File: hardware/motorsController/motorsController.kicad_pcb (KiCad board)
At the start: 2 copper layers, 166.1 x 53.6 mm, 48 parts, among them J1 batery_connector, J10 batery_connector, J11 Conn_01x04, J2 Screw_Terminal_01x01, J3 Screw_Terminal_01x01, J4 Screw_Terminal_01x01, J5 Screw_Terminal_01x01, J6 Screw_Terminal_01x01, J7 Screw_Terminal_01x01, J8 Screw_Terminal_01x01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

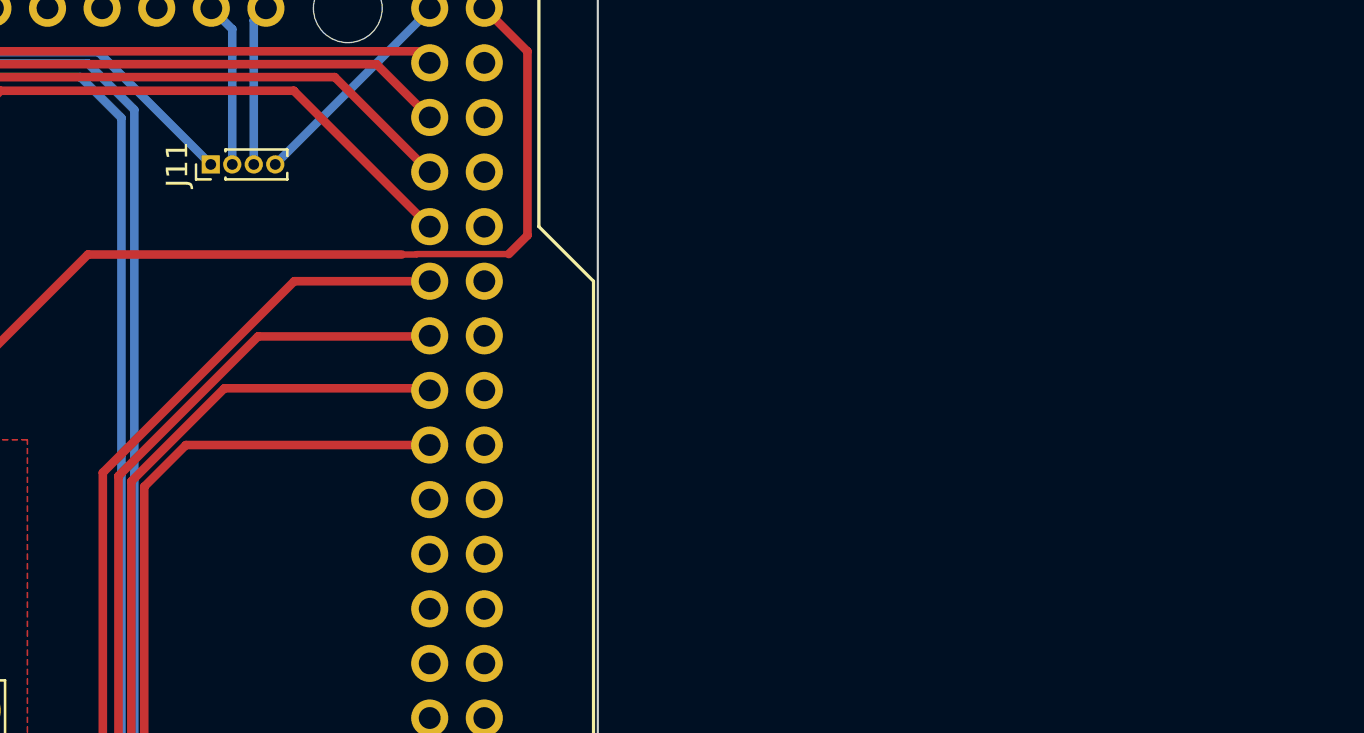
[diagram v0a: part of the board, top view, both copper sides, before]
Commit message: layout filters for an encoder
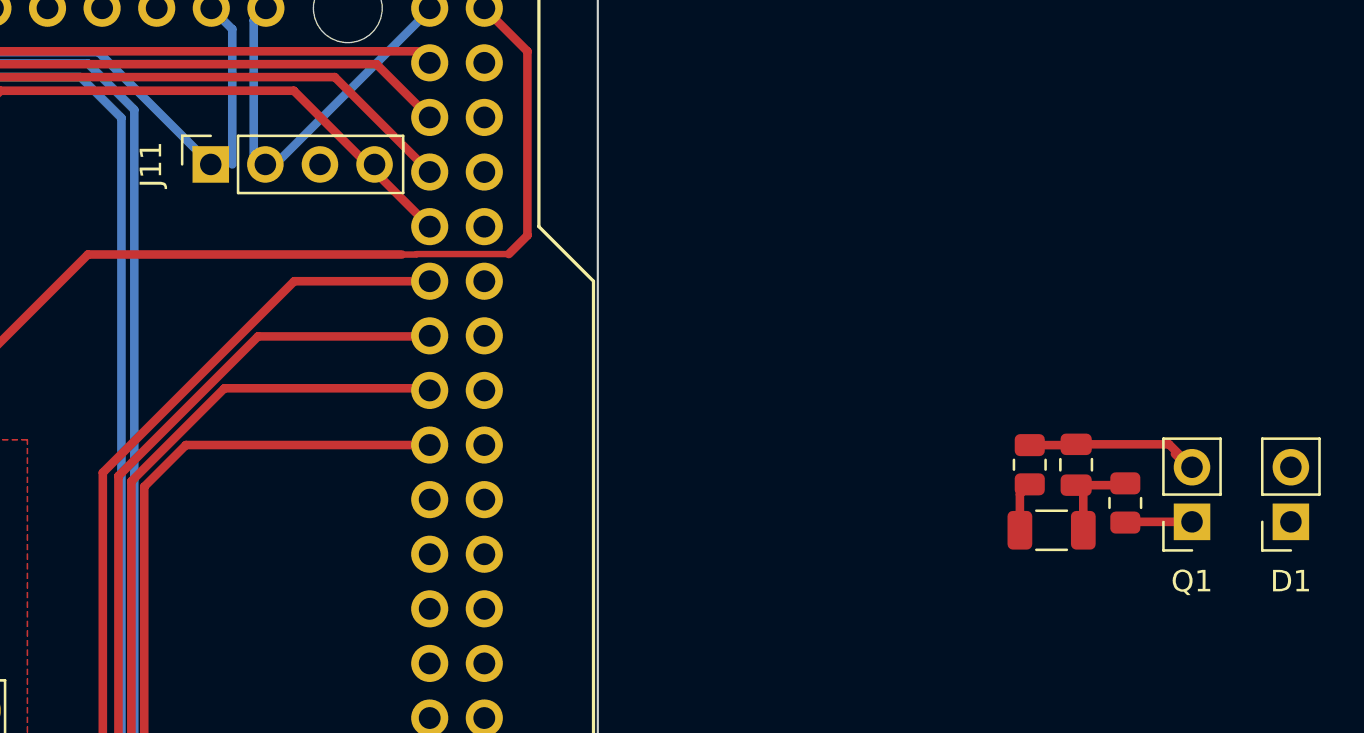
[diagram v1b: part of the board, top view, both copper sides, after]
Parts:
- added C5: 300pF, Capacitor_SMD:C_0805_2012Metric, F.Cu at (221.2, 48.3)
- added C6: 82nF, Capacitor_SMD:C_1206_3216Metric, F.Cu at (220.1, 51.3)
- added D1: LED, Connector_PinSocket_2.54mm:PinSocket_1x02_P2.54mm_Vertical, F.Cu at (231.2, 50.9)
- added Q1: Q_Photo_NPN, Connector_PinSocket_2.54mm:PinSocket_1x02_P2.54mm_Vertical, F.Cu at (226.6, 50.9)
- added R30: 2M, Resistor_SMD:R_0805_2012Metric, F.Cu at (219.1, 48.3)
- added Re: 2M, Resistor_SMD:R_0805_2012Metric, F.Cu at (223.5, 50.0)
- J11: footprint Connector_PinHeader_1.00mm:PinHeader_1x04_P1.00mm_Vertical -> Connector_PinSocket_2.54mm:PinSocket_1x04_P2.54mm_Vertical
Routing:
- net GND: track 638.6 -> 647.6 mm
- net Net-(C5-Pad1): track 0.00 -> 4.56 mm
- net Net-(Q1-Pad1): track 0.00 -> 3.13 mm
- net /front_right_encoder/out: track 0.00 -> 2.33 mm

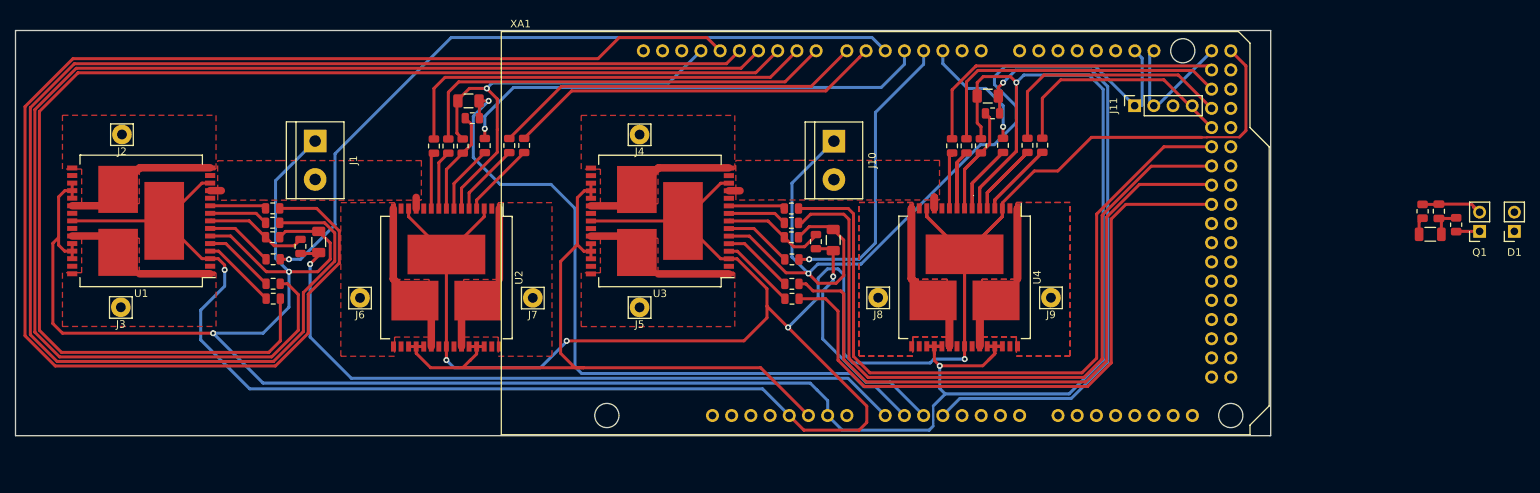
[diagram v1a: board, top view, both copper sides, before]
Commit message: connect encoder to arduino
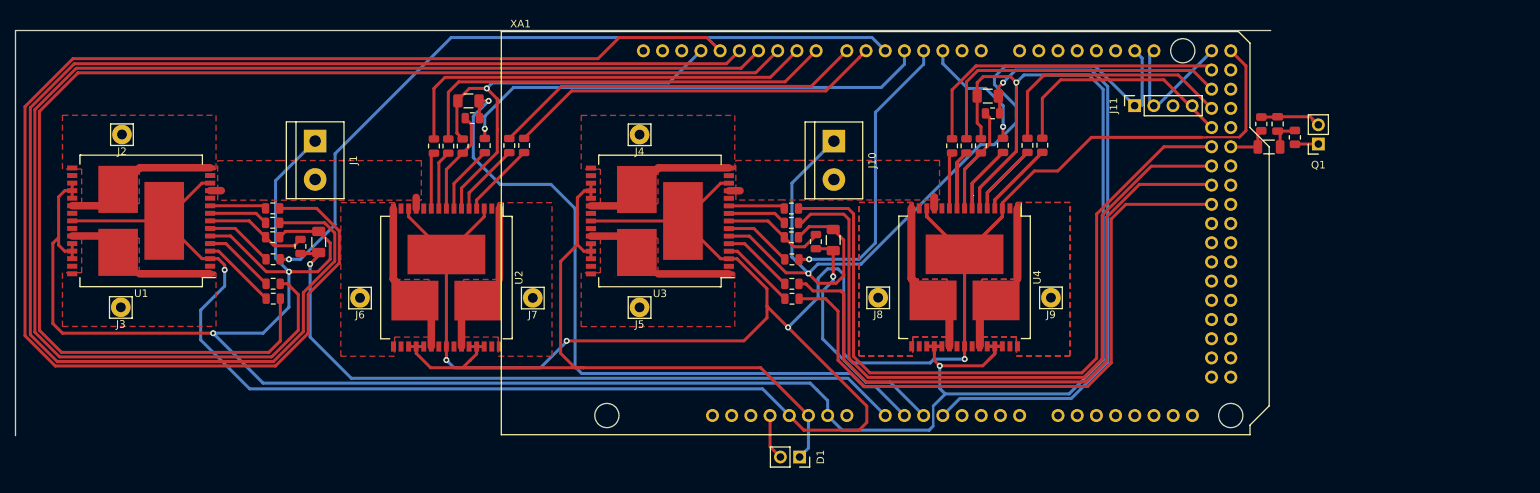
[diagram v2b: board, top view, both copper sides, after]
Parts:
- moved D1 99.2 mm to (136.7, 80.8), turned to 270 degrees
- moved C5 24.3 mm to (199.9, 36.7)
- moved C6 24.3 mm to (198.8, 39.8)
- moved R29 24.3 mm to (202.2, 38.5)
- moved Q1 24.3 mm to (205.3, 39.4)
- moved R30 24.3 mm to (197.7, 36.7)
- renumbered Re to R29
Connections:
- C6 pad 1: /front_right_encoder/out -> /front_right_encoder
- R30 pad 1: /front_right_encoder/out -> /front_right_encoder
- XA1 pad 3V3: Net-(XA1-Pad3V3) -> +3V3
- XA1 pad D31: Net-(XA1-PadD31) -> /front_right_encoder
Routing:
- net +3V3: track 0.00 -> 6.06 mm
- net GND: track 647.6 -> 653.6 mm
- net /front_right_encoder: track 0.00 -> 5.92 mm
- net /front_right_encoder/out: track 2.33 -> 0.00 mm
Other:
- outline, holes or cut-outs redrawn

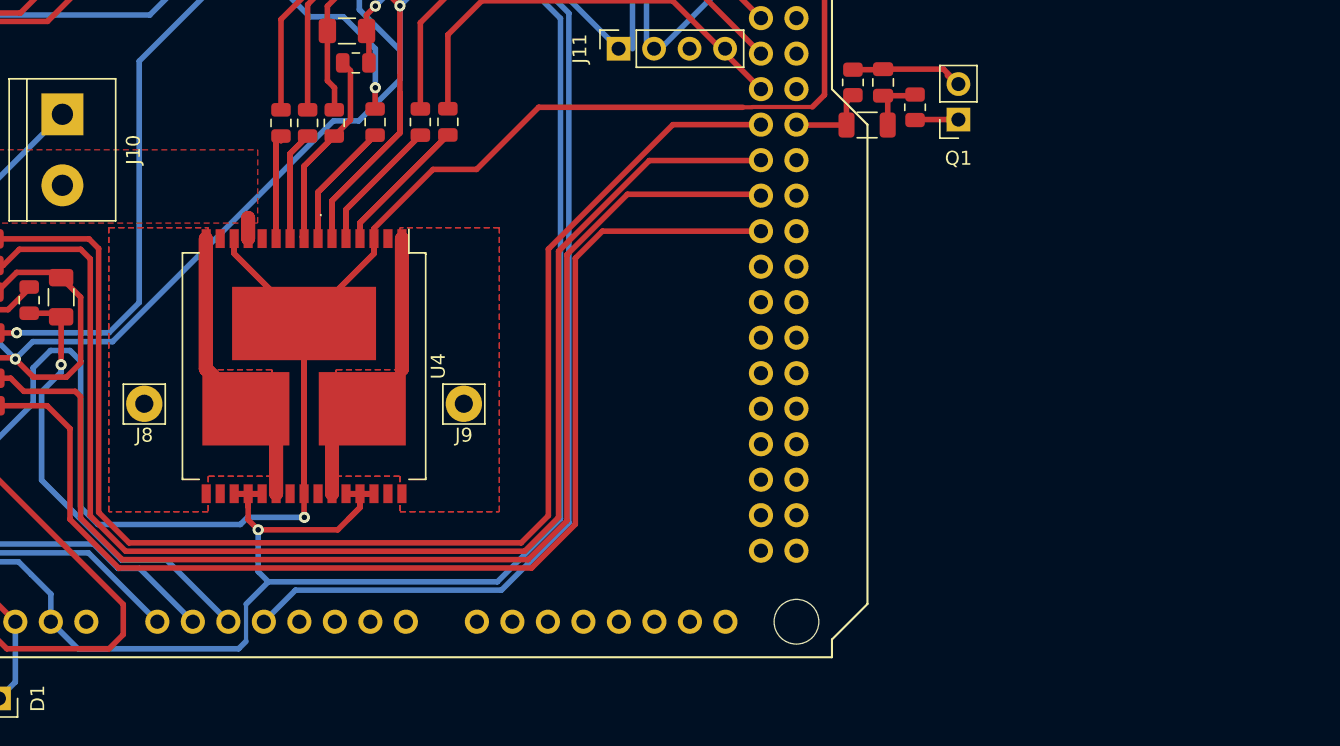
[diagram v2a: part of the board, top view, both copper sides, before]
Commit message: replicate layout for the rest of encoders
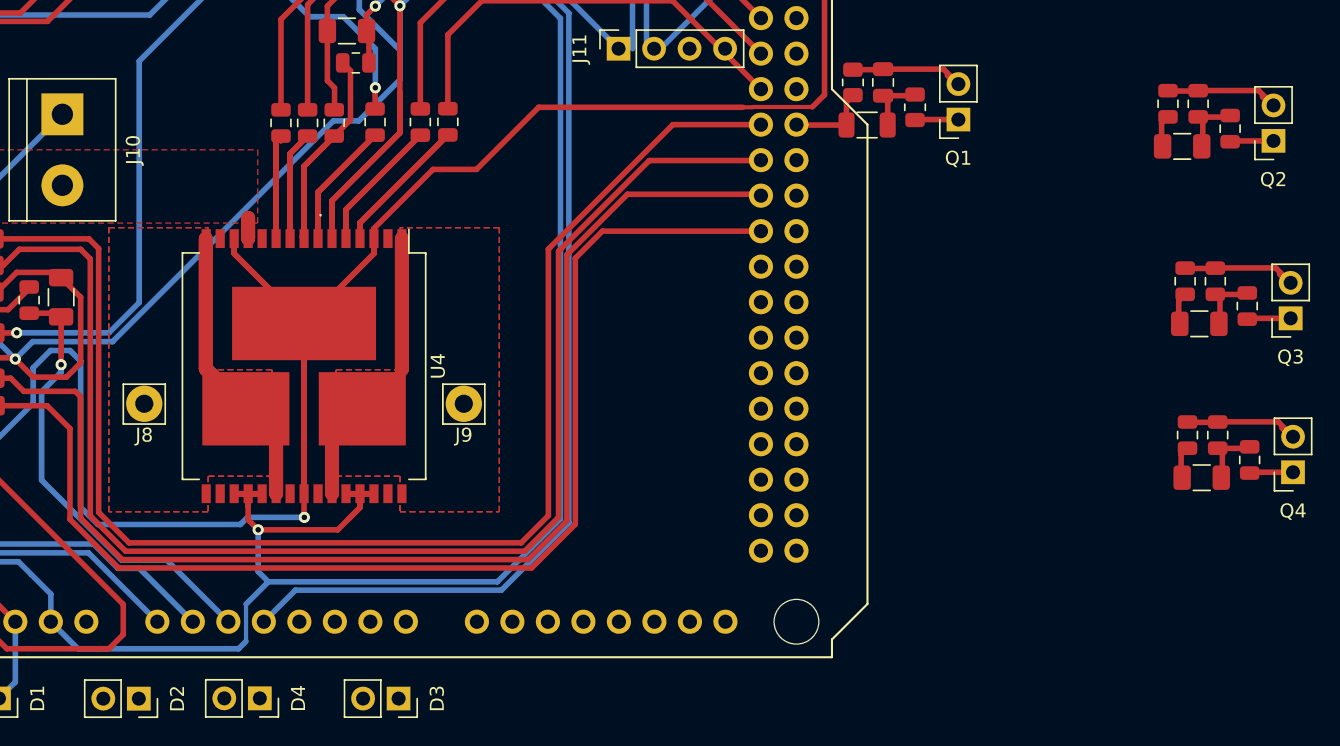
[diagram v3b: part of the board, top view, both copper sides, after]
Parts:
- added C10: 82nF, Capacitor_SMD:C_1206_3216Metric, F.Cu at (222.5, 54.0)
- added C11: 300pF, Capacitor_SMD:C_0805_2012Metric, F.Cu at (223.8, 61.9)
- added C12: 82nF, Capacitor_SMD:C_1206_3216Metric, F.Cu at (222.7, 65.0)
- added C7: 300pF, Capacitor_SMD:C_0805_2012Metric, F.Cu at (222.4, 38.2)
- added C8: 82nF, Capacitor_SMD:C_1206_3216Metric, F.Cu at (221.3, 41.3)
- added C9: 300pF, Capacitor_SMD:C_0805_2012Metric, F.Cu at (223.7, 50.9)
- added D2: LED, Connector_PinSocket_2.54mm:PinSocket_1x02_P2.54mm_Vertical, F.Cu at (146.7, 80.8)
- added D3: LED, Connector_PinSocket_2.54mm:PinSocket_1x02_P2.54mm_Vertical, F.Cu at (165.2, 80.8)
- added D4: LED, Connector_PinSocket_2.54mm:PinSocket_1x02_P2.54mm_Vertical, F.Cu at (155.3, 80.8)
- added Q2: Q_Photo_NPN, Connector_PinSocket_2.54mm:PinSocket_1x02_P2.54mm_Vertical, F.Cu at (227.8, 40.9)
- added Q3: Q_Photo_NPN, Connector_PinSocket_2.54mm:PinSocket_1x02_P2.54mm_Vertical, F.Cu at (229.1, 53.6)
- added Q4: Q_Photo_NPN, Connector_PinSocket_2.54mm:PinSocket_1x02_P2.54mm_Vertical, F.Cu at (229.2, 64.6)
- added R31: 2M, Resistor_SMD:R_0805_2012Metric, F.Cu at (224.7, 40.0)
- added R32: 2M, Resistor_SMD:R_0805_2012Metric, F.Cu at (220.3, 38.2)
- added R33: 2M, Resistor_SMD:R_0805_2012Metric, F.Cu at (226.0, 52.7)
- added R34: 2M, Resistor_SMD:R_0805_2012Metric, F.Cu at (221.5, 50.9)
- added R35: 2M, Resistor_SMD:R_0805_2012Metric, F.Cu at (226.1, 63.7)
- added R36: 2M, Resistor_SMD:R_0805_2012Metric, F.Cu at (221.7, 61.9)
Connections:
- XA1 pad D33: Net-(XA1-PadD33) -> /front_left_encoder
- XA1 pad D35: Net-(XA1-PadD35) -> /rear_right_encoder
- XA1 pad D37: Net-(XA1-PadD37) -> /rear_left_encoder
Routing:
- net GND: track 653.6 -> 680.8 mm
- net Net-(C11-Pad1): track 0.00 -> 4.56 mm
- net Net-(C10-Pad2): track 0.00 -> 4.56 mm
- net Net-(C7-Pad1): track 0.00 -> 4.56 mm
- net Net-(Q4-Pad1): track 0.00 -> 3.13 mm
- net Net-(Q3-Pad1): track 0.00 -> 3.13 mm
- net Net-(Q2-Pad1): track 0.00 -> 3.13 mm
- net /rear_left_encoder: track 0.00 -> 2.33 mm
- net /rear_right_encoder: track 0.00 -> 2.33 mm
- net /front_left_encoder: track 0.00 -> 2.33 mm

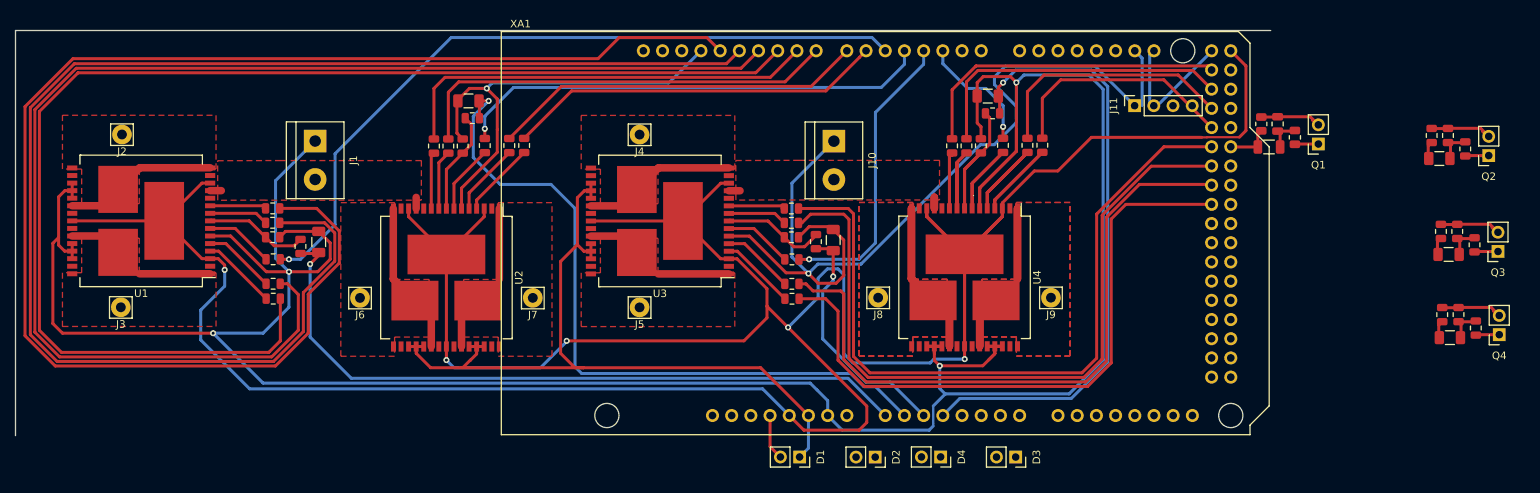
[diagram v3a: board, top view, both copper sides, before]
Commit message: place and connect the rest of encoders
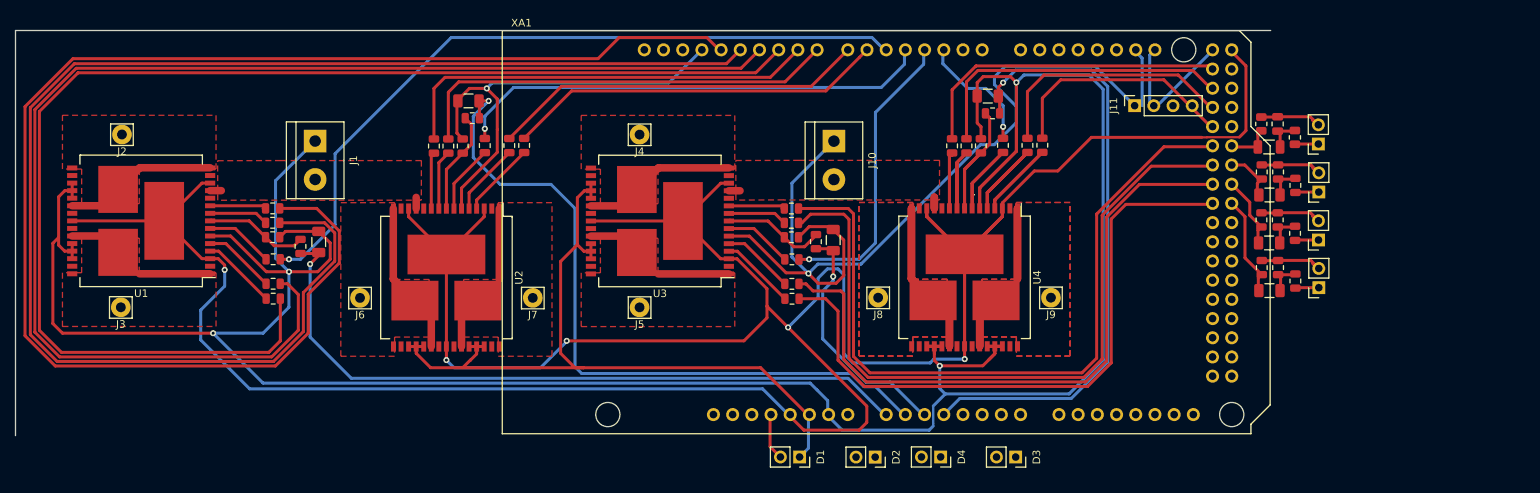
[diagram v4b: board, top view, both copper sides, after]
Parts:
- moved C11 24.7 mm to (200.0, 55.7)
- moved C12 24.7 mm to (198.8, 58.8)
- moved Q4 24.7 mm to (205.3, 58.4)
- moved R35 24.7 mm to (202.2, 57.5)
- moved R36 24.7 mm to (197.8, 55.7)
- moved C10 23.8 mm to (198.8, 52.4)
- moved C9 23.8 mm to (199.9, 49.4)
- moved Q3 23.8 mm to (205.3, 52.1)
- moved R33 23.8 mm to (202.2, 51.2)
- moved R34 23.8 mm to (197.8, 49.4)
- moved C7 23.0 mm to (200.0, 43.1)
- moved C8 23.0 mm to (198.8, 46.1)
- moved R31 23.0 mm to (202.2, 44.8)
- moved Q2 23.0 mm to (205.3, 45.7)
- moved R32 23.0 mm to (197.8, 43.1)
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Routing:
- net /rear_left_encoder: track 2.33 -> 13.4 mm
- net /rear_right_encoder: track 2.33 -> 9.61 mm
- net /front_left_encoder: track 2.33 -> 7.07 mm
